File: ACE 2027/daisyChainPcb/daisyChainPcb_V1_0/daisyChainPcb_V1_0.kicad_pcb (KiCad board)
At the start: 2 copper layers, 56.5 x 97 mm, 26 parts, among them J201 Pads, J202 XT30, J203 XT30, J204 Pads, J205 Pads, J206 RJ45, J207 RJ45, U101 AP7361C-33E-13

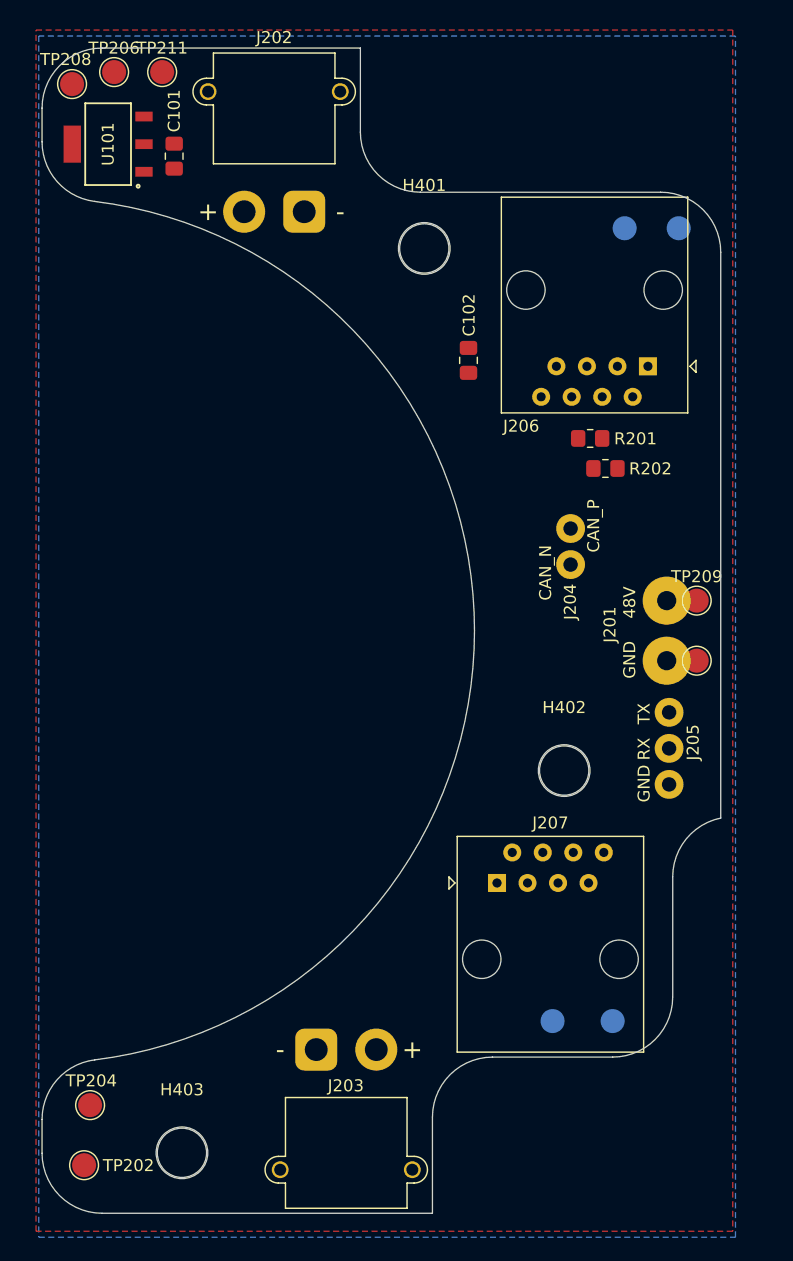
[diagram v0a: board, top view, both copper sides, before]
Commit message: Finished routing the pcb I want to clean up the silkscreen before saying it is finished
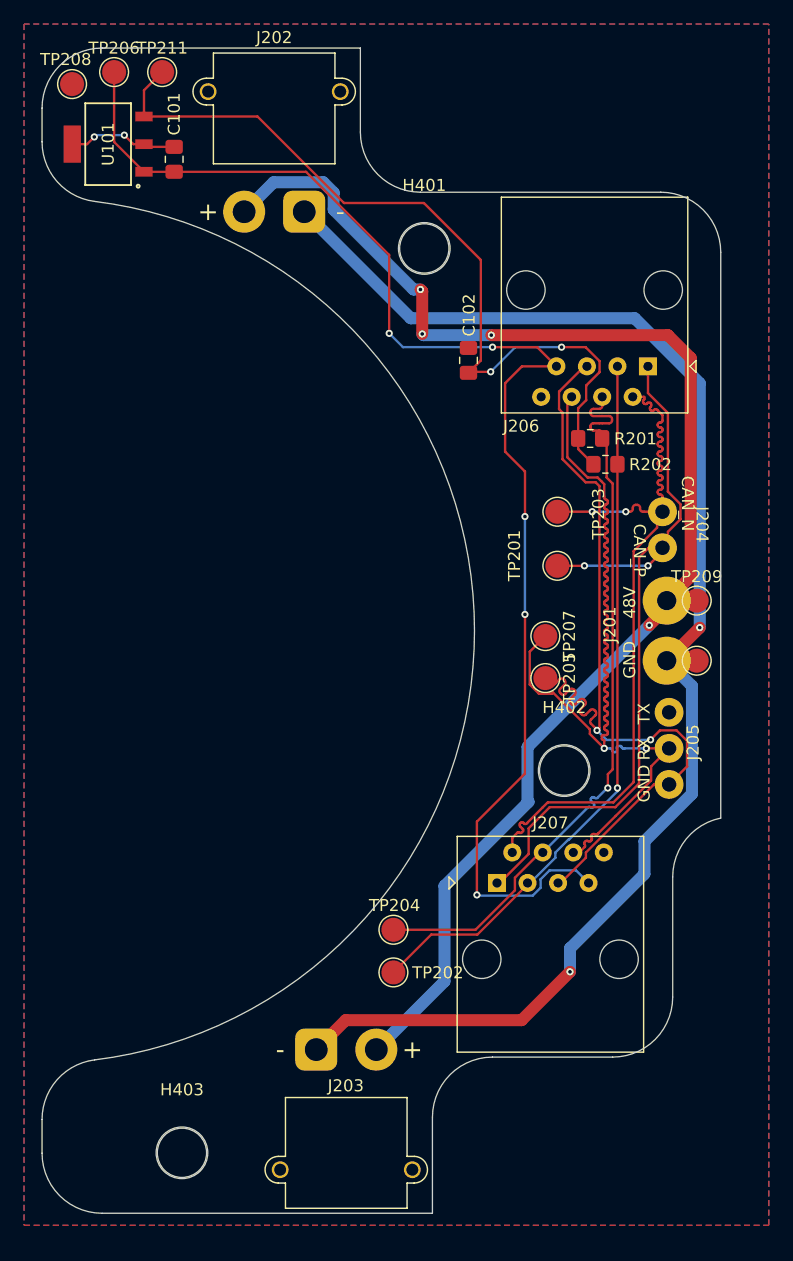
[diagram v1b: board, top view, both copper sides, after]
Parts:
- TP201, TP203, TP205, TP207: moved to F.Cu
- moved TP207 32.5 mm to (166.4, 88.0), turned to -90 degrees
- moved TP202 30.3 mm to (153.8, 116.0)
- moved TP201 29.9 mm to (167.4, 82.1), turned to 90 degrees
- moved TP204 29.2 mm to (153.8, 112.4)
- moved TP205 28.6 mm to (166.4, 91.5), turned to -90 degrees
- moved TP203 24.3 mm to (167.4, 77.6), turned to 90 degrees
- moved J204 8.83 mm to (176.2, 77.6), turned to -90 degrees
- moved R202 0.35 mm to (171.4, 73.7)
- moved C101 0.26 mm to (135.5, 48.3)
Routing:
- net power_GND: track 0.00 -> 120.4 mm, vias 0 -> 2
- net +48V: track 0.00 -> 118.1 mm, vias 0 -> 4
- net +5V: track 0.00 -> 115.0 mm, vias 0 -> 5
- net /Controle/RX: track 0.00 -> 72.4 mm, vias 0 -> 2
- net /Controle/TX: track 0.00 -> 71.3 mm, vias 0 -> 2
- net VCC_3V3: track 0.00 -> 69.3 mm, vias 0 -> 2
- net /Controle/CAN_P: track 0.00 -> 64.0 mm, vias 0 -> 2
- net /Controle/CAN_N: track 0.00 -> 63.5 mm, vias 0 -> 2
- net /Controle/SCL: track 0.00 -> 61.9 mm, vias 0 -> 1
- net /Controle/SDA: track 0.00 -> 60.6 mm, vias 0 -> 1
- net signal_GND: track 0.00 -> 9.20 mm, vias 0 -> 2
- added copper zone on B.Cu, net signal_GND
- removed copper zone on B.Cu, net power_GND

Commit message: Finished silkscreen
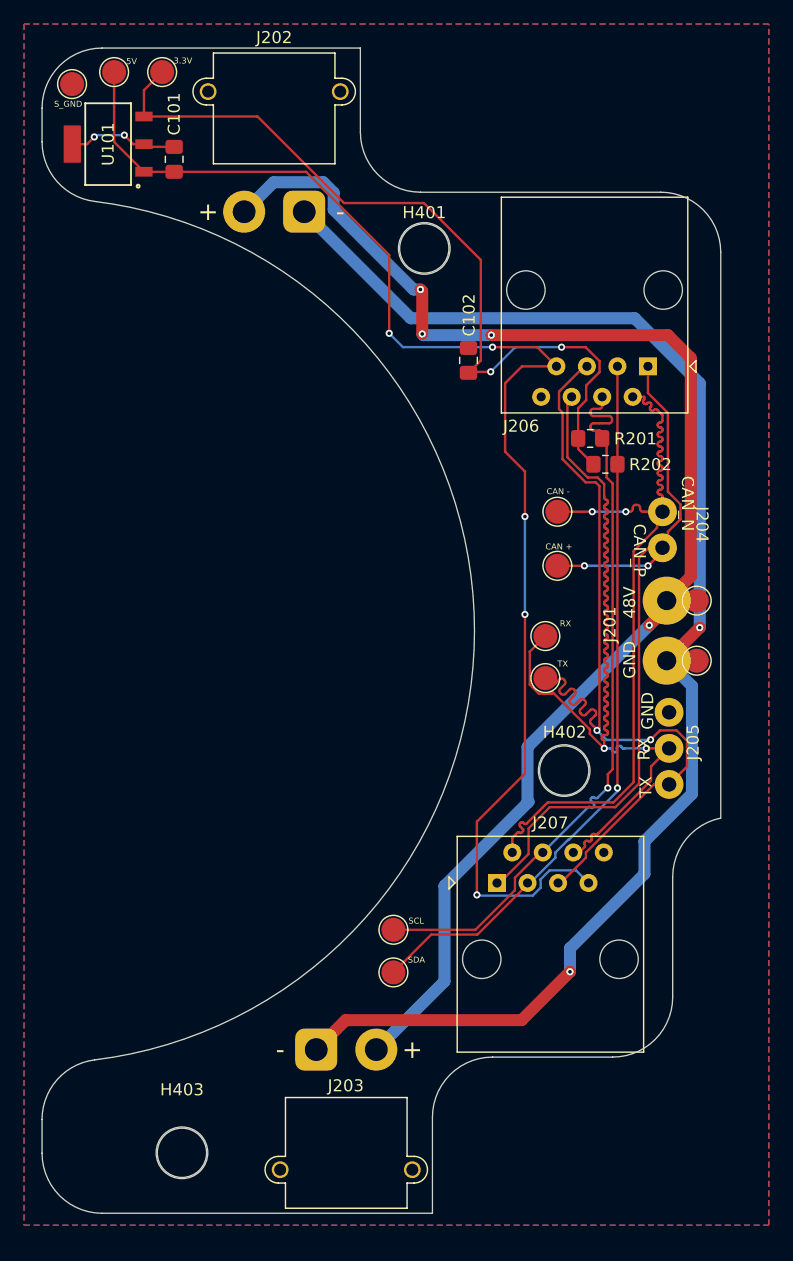
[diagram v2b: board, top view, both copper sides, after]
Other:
- board text added: "3.3V"
- board text added: "5V"
- board text added: "CAN +"
- board text added: "CAN -"
- board text added: "RX"
- board text added: "SCL"
- board text added: "SDA"
- board text added: "S_GND"
- board text added: "TX"
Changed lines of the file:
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@@
 		(property "Reference" "TP204"
 			(at 0.1 -2.025 0)
-			(layer "F.SilkS")
+			(layer "F.Fab")
 			(effects
 				(font
@@
 		(attr smd)
 		(duplicate_pad_numbers_are_jumpers no)
-		(fp_text user "TX"
-			(at 5 -1.5 90)
+		(fp_text user "RX"
+			(at 2 -1.5 90)
 			(unlocked yes)
 			(layer "F.SilkS")
@@
 			)
 		)
-		(fp_text user "RX"
-			(at 2 -1.5 90)
+		(fp_text user "TX"
+			(at -1.1 -1.35 90)
 			(unlocked yes)
 			(layer "F.SilkS")
@@
 		)
 		(fp_text user "GND"
-			(at -1.5 -1.5 90)
+			(at 4.55 -1.2 90)
 			(unlocked yes)
 			(layer "F.SilkS")
@@
 		(tags "mountinghole M4")
 		(property "Reference" "H402"
-			(at 0 -5.25 0)
+			(at 0.033338 -3.196857 0)
 			(layer "F.SilkS")
 			(effects
@@
 		(property "Reference" "TP209"
 			(at 0 -1.998 0)
-			(layer "F.SilkS")
+			(layer "F.Fab")
 			(effects
 				(font
@@
 		(property "Reference" "TP207"
 			(at 0 -1.998 90)
-			(layer "F.SilkS")
+			(layer "F.Fab")
 			(effects
 				(font
@@
 		(tags "mountinghole M4")
 		(property "Reference" "H401"
-			(at 0 -5.25 0)
+			(at 0 -2.980195 0)
 			(layer "F.SilkS")
 			(effects
@@
 		(property "Reference" "TP202"
 			(at 3.7 0.027 0)
-			(layer "F.SilkS")
+			(layer "F.Fab")
 			(effects
 				(font
@@
 		(property "Reference" "TP201"
 			(at 0.85 -3.575 90)
-			(layer "F.SilkS")
+			(layer "F.Fab")
 			(effects
 				(font
@@
 		(property "Reference" "TP203"
 			(at -0.175 3.423 90)
-			(layer "F.SilkS")
+			(layer "F.Fab")
 			(effects
 				(font
@@
 		(property "Reference" "TP208"
 			(at -0.525 -2.05 0)
-			(layer "F.SilkS")
+			(layer "F.Fab")
 			(effects
 				(font
@@
 		(property "Reference" "TP206"
 			(at 0 -1.998 0)
-			(layer "F.SilkS")
+			(layer "F.Fab")
 			(effects
 				(font
@@
 		(property "Reference" "TP205"
 			(at 0 -1.998 90)
-			(layer "F.SilkS")
+			(layer "F.Fab")
 			(effects
 				(font
@@
 		(property "Reference" "TP211"
 			(at 0 -1.998 0)
-			(layer "F.SilkS")
+			(layer "F.Fab")
 			(effects
 				(font
@@
 		(layer "Edge.Cuts")
 	)
+	(gr_text "S_GND"
+		(at 125.5 43.95 0)
+		(layer "F.SilkS")
+		(effects
+			(font
+				(size 0.5 0.5)
+				(thickness 0.1)
+			)
+			(justify left bottom)
+		)
+	)
+	(gr_text "5V"
+		(at 131.5 40.4 0)
+		(layer "F.SilkS")
+		(effects
+			(font
+				(size 0.5 0.5)
+				(thickness 0.1)
+			)
+			(justify left bottom)
+		)
+	)
+	(gr_text "3.3V"
+		(at 135.45 40.35 0)
+		(layer "F.SilkS")
+		(effects
+			(font
+				(size 0.5 0.5)
+				(thickness 0.1)
+			)
+			(justify left bottom)
+		)
+	)
+	(gr_text "SDA"
+		(at 154.95 115.2 0)
+		(layer "F.SilkS")
+		(effects
+			(font
+				(size 0.5 0.5)
+				(thickness 0.1)
+			)
+			(justify left bottom)
+		)
+	)
+	(gr_text "SCL"
+		(at 155 111.95 0)
+		(layer "F.SilkS")
+		(effects
+			(font
+				(size 0.5 0.5)
+				(thickness 0.1)
+			)
+			(justify left bottom)
+		)
+	)
+	(gr_text "CAN +"
+		(at 166.4 80.8 0)
+		(layer "F.SilkS")
+		(effects
+			(font
+				(size 0.5 0.5)
+				(thickness 0.1)
+			)
+			(justify left bottom)
+		)
+	)
+	(gr_text "CAN -"
+		(at 166.5 76.2 0)
+		(layer "F.SilkS")
+		(effects
+			(font
+				(size 0.5 0.5)
+				(thickness 0.1)
+			)
+			(justify left bottom)
+		)
+	)
+	(gr_text "TX"
+		(at 167.4 90.55 0)
+		(layer "F.SilkS")
+		(effects
+			(font
+				(size 0.5 0.5)
+				(thickness 0.1)
+			)
+			(justify left bottom)
+		)
+	)
+	(gr_text "RX"
+		(at 167.6 87.2 0)
+		(layer "F.SilkS")
+		(effects
+			(font
+				(size 0.5 0.5)
+				(thickness 0.1)
+			)
+			(justify left bottom)
+		)
+	)
 	(segment

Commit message: Added logo
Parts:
- added G***: LOGO, LOGO, F.Cu at (164.4, 74.8)
- moved TP203 1.50 mm to (167.3, 79.1)
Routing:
- net /Controle/CAN_N: track 63.5 -> 64.2 mm
- net /Controle/CAN_P: track 64.0 -> 64.6 mm
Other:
- board text added: "CAN_N"
- board text added: "CAN_P"

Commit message: Trying to fix the branch
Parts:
- moved TP208 27.4 mm to (149.2, 58.2)
- moved TP205 24.2 mm to (156.8, 113.7)
- moved TP207 24.2 mm to (156.8, 110.2)
- moved TP204 22.3 mm to (134.8, 124.2), turned to 90 degrees
- moved TP202 17.4 mm to (138.3, 124.2), turned to 90 degrees
- moved TP203 7.82 mm to (165.8, 71.5)
- moved G*** 7.40 mm to (166.8, 81.8)
- moved TP201 7.24 mm to (165.8, 75.0)
- moved TP206 2.25 mm to (128.3, 41.5)
- moved TP211 0.95 mm to (133.6, 41.0)
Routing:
- net /Controle/SDA: track 60.6 -> 86.7 mm, vias 1 -> 2
- net /Controle/SCL: track 61.9 -> 86.8 mm, vias 1 -> 2
- net /Controle/CAN_N: track 64.2 -> 75.2 mm
- net signal_GND: track 9.20 -> 19.4 mm, vias 2 -> 413
- net /Controle/TX: track 71.3 -> 78.2 mm, vias 2 -> 3
- net /Controle/RX: track 72.4 -> 77.9 mm, vias 2 -> 3
- net +5V: track 115.0 -> 115.9 mm, vias 5 -> 7
- net /Controle/CAN_P: track 64.6 -> 65.4 mm
- net VCC_3V3: track 69.3 -> 68.8 mm, vias 2 -> 4
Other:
- board text added: "5V to 3.3V"
- board text added: "CAN+"
- board text added: "CAN-"
- board text added: "Créé par: Samuel Archambault"
- board text added: "Pull ups I2C"
- board text removed: "CAN +"
- board text removed: "CAN -"

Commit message: Réglé le placement de certain silkscreen et les vias du stiching
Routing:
- net signal_GND: vias 413 -> 229
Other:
- board text added: "+"
- board text added: "-"

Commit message: Halfway through better placing the TP
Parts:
- TP205, TP207: moved to B.Cu
- moved TP201 23.7 mm to (161.8, 98.5)
- moved TP203 23.7 mm to (161.8, 94.8)
- moved TP205 16.8 mm to (172.6, 119.2), turned to 0 degrees
- moved TP207 15.3 mm to (169.1, 119.2), turned to 0 degrees
- moved TP202 11.3 mm to (129.4, 131.1), turned to 0 degrees
- moved TP204 6.34 mm to (129.4, 127.5), turned to 0 degrees
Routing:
- net /Controle/CAN_P: track 65.4 -> 54.5 mm, vias 2 -> 1
- net /Controle/SCL: track 86.8 -> 94.1 mm
- net /Controle/SDA: track 86.7 -> 93.7 mm
- net /Controle/CAN_N: track 75.2 -> 70.8 mm, vias 2 -> 0
- net /Controle/RX: track 77.9 -> 75.4 mm, vias 3 -> 2
- net /Controle/TX: track 78.2 -> 76.3 mm, vias 3 -> 2
- net signal_GND: vias 229 -> 2
